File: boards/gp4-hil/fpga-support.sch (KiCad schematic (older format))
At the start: 56 parts, among them J2 XILINX_JTAG, U2 XC7A100T-1FTG256C, U6 W25Q32FW

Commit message: Wired up FPGA config pins, flash, etc
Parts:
- added C143: 4.7 uF, symbol C
- added C144: 0.47 uF, symbol C
- added R119, R120: 1K, symbol R
- added R121, R122, R123, R124, R125, R126, R127, R128, R129, R133, R134: 33, symbol R
- added R130, R131, R132: 4.7K, symbol R
- added R? (x3): 0, symbol R
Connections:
- net 1V0: now also U2.E10 (VCCBRAM), U2.F11 (VCCBRAM), U2.F7 (VCCINT), U2.F9 (VCCINT), U2.G6 (VCCINT), U2.H9 (VCCINT), U2.J6 (VCCINT), U2.K9 (VCCINT), U2.L8 (VCCINT)
- net 1V8: now also C100.1, C104.1, C108.1, C112.1, C87.1, C88.1, C92.1, C96.1, J2.2 (Vccaux), U2.F8 (VCCBATT), U2.G10 (VCCAUX), U2.G8 (VCCADC), U2.J10 (VCCAUX), U2.K11 (VCCAUX), U2.L10 (VCCAUX), U2.L16 (VCCO_14), U2.L6 (VCCO_0), U2.M13 (VCCO_14), U2.N10 (VCCO_14), U2.P7 (VCCO_14), U2.R14 (VCCO_14), U2.T11 (VCCO_14), U6.8 (VCC), C143.2, C144.2, R119.2, R120.2, R130.1, R131.1, R132.1, R?.2
- net 2V5: now also C101.1, C105.1, C109.1, C113.1, C89.1, C93.1, C97.1, U2.A16 (VCCO_15), U2.B13 (VCCO_15), U2.C10 (VCCO_15), U2.E14 (VCCO_15), U2.H15 (VCCO_15), U2.J12 (VCCO_15)
- net DUT_VDD1: now also C103.1, C107.1, C111.1, C115.1, C91.1, C95.1, C99.1, U2.A6 (VCCO_35), U2.B3 (VCCO_35), U2.D7 (VCCO_35), U2.E4 (VCCO_35), U2.F1 (VCCO_35), U2.J2 (VCCO_35)
- net DUT_VDD2: now also C102.1, C106.1, C110.1, C114.1, C90.1, C94.1, C98.1, U2.M3 (VCCO_34), U2.R4 (VCCO_34), U2.T1 (VCCO_34)
- net GND: now also J2.11 (Vss), J2.3 (Vss), J2.5 (Vss), J2.7 (Vss), J2.9 (Vss), U2.E7 (CFGBVS), U2.H7 (XADC_VREF_N), U2.H8 (XADC_VP), U2.J7 (XADC_VN), U2.J8 (XADC_VREF_P), U2.K7 (THERMAL_D_N), U2.K8 (THERMAL_D_P), U6.4 (GND), C143.1, C144.1, R?.2, R?.2
- net FLASH_SCK: now reaches U2.E8 (CCLK)
- net FLASH_SCK: now also R129.2
- net FPGA_DONE: now reaches U2.H10 (DONE)
- net FPGA_DONE: now also R119.1
- net FPGA_INIT_B: now reaches U2.K10 (INIT_B)
- net FPGA_INIT_B: now also R120.1
- net JTAG_TCK: now reaches U2.L7 (TCK)
- net JTAG_TCK: now also J2.6 (TCK)
- net PSU_PGOOD: now reaches U2.L9 (PROG_B)
- net at U2.M10 (M1): now also R?.1
- net at U2.M11 (M2): now also R?.1
- net JTAG_TMS: now reaches U2.M7 (TMS)
- net JTAG_TMS: now also J2.4 (TMS)
- net at U2.M9 (M0): now also R?.1
- net JTAG_TDI: now reaches U2.N7 (TDI)
- net JTAG_TDI: now also J2.10 (TDI_OUT)
- net at U2.N8 (TDO): now also R121.1
- net FLASH_CS_NT: now reaches U6.1 (CS#)
- net FLASH_CS_NT: now also R124.1, R130.2
- net at U6.2 (DO/IO1): now also R122.1
- net at U6.3 (WP#/IO2): now also R123.1
- net at U6.5 (DI/IO0): now also R134.2
- net FLASH_SCKT: now reaches U6.6 (CLK)
- net FLASH_SCKT: now also R129.1
- net at U6.7 (HOLD#/IO3): now also R133.2
- net JTAG_TDO: now reaches J2.8 (TDO_IN)
- net JTAG_TDO: now also R121.2
- new net FLASH_CS_N: R124.2
- new net FLASH_DQ0: R128.2
- new net FLASH_DQ0T: R128.1, R134.1
- new net FLASH_DQ1: R127.2
- new net FLASH_DQ1T: R122.2, R127.1
- new net FLASH_DQ2: R126.2
- new net FLASH_DQ2T: R123.2, R126.1, R132.2
- new net FLASH_DQ3: R125.2
- new net FLASH_DQ3T: R125.1, R131.2, R133.1
- no-connect marks 0 -> 2
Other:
- moved on the sheet: J2

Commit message: Added lots of analog I/O stuff
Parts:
- gave numbers to parts that had none: 3
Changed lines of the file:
@@
 Connection ~ 7750 9250
 $Comp
-L R R?
+L R R135
 U 1 1 57495D86
 P 7200 10750
-F 0 "R?" V 7150 10950 50  0000 C CNN
+F 0 "R135" V 7150 10950 50  0000 C CNN
 F 1 "0" V 7200 10750 50  0000 C CNN
 F 2 "" V 7130 10750 30  0000 C CNN
@@
 	7350 10750 7850 10750
 $Comp
-L R R?
+L R R136
 U 1 1 5749642D
 P 7200 10850
-F 0 "R?" V 7150 11050 50  0000 C CNN
+F 0 "R136" V 7150 11050 50  0000 C CNN
 F 1 "0" V 7200 10850 50  0000 C CNN
 F 2 "" V 7130 10850 30  0000 C CNN
@@
 $EndComp
 $Comp
-L R R?
+L R R137
 U 1 1 57496524
 P 7200 10950
-F 0 "R?" V 7150 11150 50  0000 C CNN
+F 0 "R137" V 7150 11150 50  0000 C CNN
 F 1 "0" V 7200 10950 50  0000 C CNN
 F 2 "" V 7130 10950 30  0000 C CNN

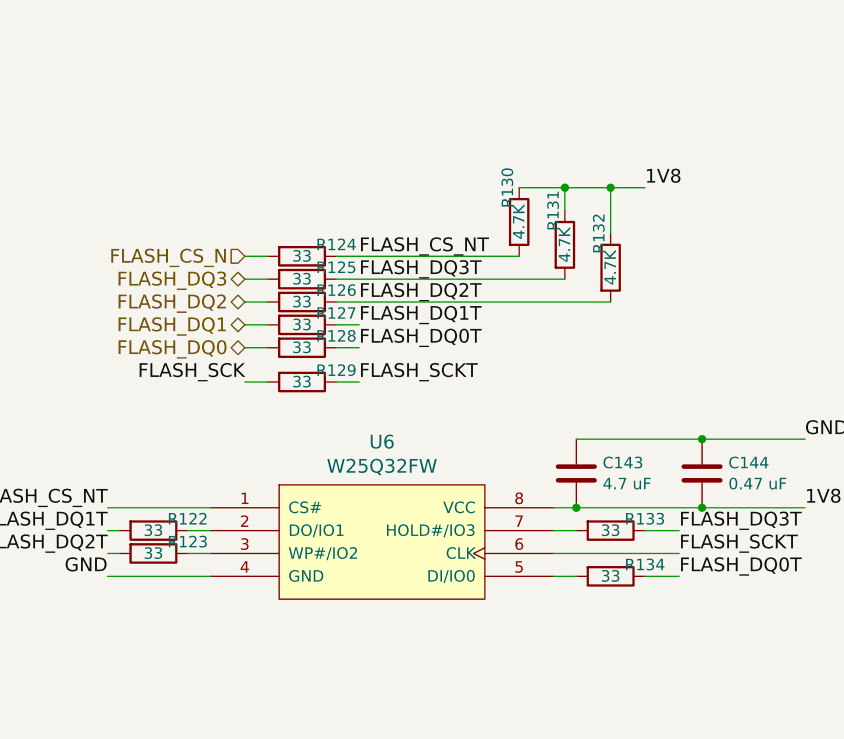
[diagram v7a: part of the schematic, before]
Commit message: Minor refdes placement tweaks
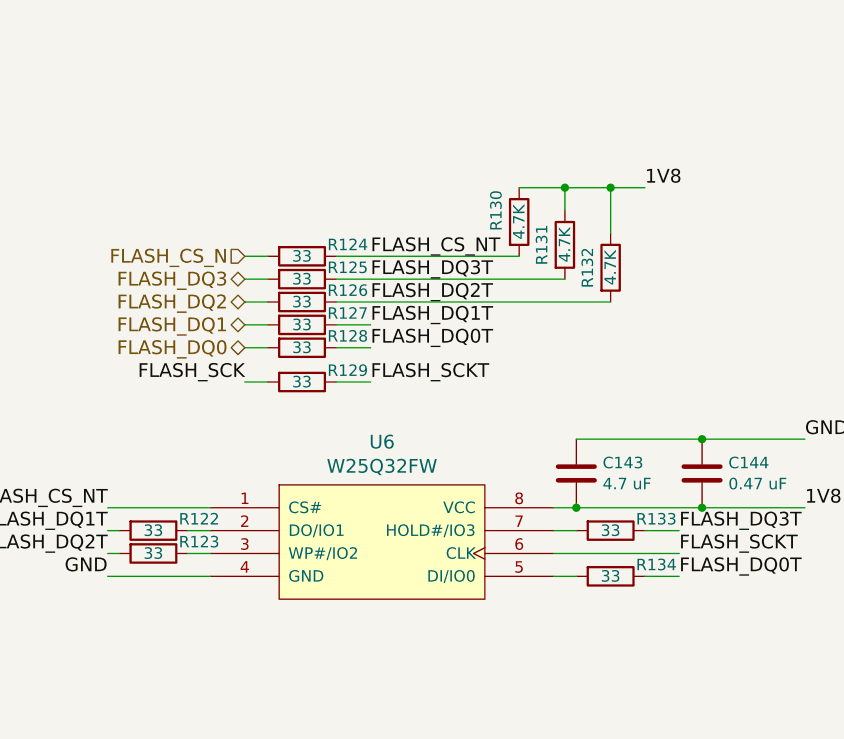
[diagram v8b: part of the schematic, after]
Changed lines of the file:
@@
 U 1 1 5748A020
 P 17550 8600
-F 0 "R122" V 17500 8750 50  0000 C CNN
+F 0 "R122" V 17500 8800 50  0000 C CNN
 F 1 "33" V 17550 8600 50  0000 C CNN
 F 2 "" V 17480 8600 30  0000 C CNN
@@
 U 1 1 5748A79A
 P 17550 8700
-F 0 "R123" V 17500 8850 50  0000 C CNN
+F 0 "R123" V 17500 8900 50  0000 C CNN
 F 1 "33" V 17550 8700 50  0000 C CNN
 F 2 "" V 17480 8700 30  0000 C CNN
@@
 U 1 1 5748A9A0
 P 18200 7400
-F 0 "R124" V 18150 7550 50  0000 C CNN
+F 0 "R124" V 18150 7600 50  0000 C CNN
 F 1 "33" V 18200 7400 50  0000 C CNN
 F 2 "" V 18130 7400 30  0000 C CNN
@@
 U 1 1 5748ACEF
 P 18200 7500
-F 0 "R125" V 18150 7650 50  0000 C CNN
+F 0 "R125" V 18150 7700 50  0000 C CNN
 F 1 "33" V 18200 7500 50  0000 C CNN
 F 2 "" V 18130 7500 30  0000 C CNN
@@
 U 1 1 5748ADFF
 P 18200 7600
-F 0 "R126" V 18150 7750 50  0000 C CNN
+F 0 "R126" V 18150 7800 50  0000 C CNN
 F 1 "33" V 18200 7600 50  0000 C CNN
 F 2 "" V 18130 7600 30  0000 C CNN
@@
 U 1 1 5748AF99
 P 18200 7700
-F 0 "R127" V 18150 7850 50  0000 C CNN
+F 0 "R127" V 18150 7900 50  0000 C CNN
 F 1 "33" V 18200 7700 50  0000 C CNN
 F 2 "" V 18130 7700 30  0000 C CNN
@@
 U 1 1 5748B0B1
 P 18200 7800
-F 0 "R128" V 18150 7950 50  0000 C CNN
+F 0 "R128" V 18150 8000 50  0000 C CNN
 F 1 "33" V 18200 7800 50  0000 C CNN
 F 2 "" V 18130 7800 30  0000 C CNN
@@
 Wire Wire Line
 	17950 7800 18050 7800
-Text Label 18450 7400 0    60   ~ 0
+Text Label 18500 7400 0    60   ~ 0
 FLASH_CS_NT
 Wire Wire Line
 	18350 7400 19150 7400
-Text Label 18450 7500 0    60   ~ 0
+Text Label 18500 7500 0    60   ~ 0
 FLASH_DQ3T
-Text Label 18450 7600 0    60   ~ 0
+Text Label 18500 7600 0    60   ~ 0
 FLASH_DQ2T
-Text Label 18450 7700 0    60   ~ 0
+Text Label 18500 7700 0    60   ~ 0
 FLASH_DQ1T
-Text Label 18450 7800 0    60   ~ 0
+Text Label 18500 7800 0    60   ~ 0
 FLASH_DQ0T
 Wire Wire Line
@@
 	18350 7600 19550 7600
 Wire Wire Line
-	18350 7700 18450 7700
-Wire Wire Line
-	18450 7800 18350 7800
+	18350 7700 18500 7700
+Wire Wire Line
+	18350 7800 18500 7800
 $Comp
 L C C143
@@
 U 1 1 5748DD5A
 P 19550 8600
-F 0 "R133" V 19500 8750 50  0000 C CNN
+F 0 "R133" V 19500 8800 50  0000 C CNN
 F 1 "33" V 19550 8600 50  0000 C CNN
 F 2 "" V 19480 8600 30  0000 C CNN
@@
 U 1 1 5748E267
 P 19550 8800
-F 0 "R134" V 19500 8950 50  0000 C CNN
+F 0 "R134" V 19500 9000 50  0000 C CNN
 F 1 "33" V 19550 8800 50  0000 C CNN
 F 2 "" V 19480 8800 30  0000 C CNN
@@
 U 1 1 5748F616
 P 18200 7950
-F 0 "R129" V 18150 8100 50  0000 C CNN
+F 0 "R129" V 18150 8150 50  0000 C CNN
 F 1 "33" V 18200 7950 50  0000 C CNN
 F 2 "" V 18130 7950 30  0000 C CNN
@@
 Text Label 17950 7950 2    60   ~ 0
 FLASH_SCK
-Text Label 18450 7950 0    60   ~ 0
+Text Label 18500 7950 0    60   ~ 0
 FLASH_SCKT
 Wire Wire Line
-	18450 7950 18350 7950
+	18350 7950 18500 7950
 Text Label 19850 8700 0    60   ~ 0
 FLASH_SCKT
@@
 U 1 1 574915B1
 P 19550 7450
-F 0 "R132" V 19500 7600 50  0000 C CNN
+F 0 "R132" V 19450 7450 50  0000 C CNN
 F 1 "4.7K" V 19550 7450 50  0000 C CNN
 F 2 "" V 19480 7450 30  0000 C CNN
@@
 U 1 1 57491A07
 P 19350 7350
-F 0 "R131" V 19300 7500 50  0000 C CNN
+F 0 "R131" V 19250 7350 50  0000 C CNN
 F 1 "4.7K" V 19350 7350 50  0000 C CNN
 F 2 "" V 19280 7350 30  0000 C CNN
@@
 U 1 1 57492BFD
 P 19150 7250
-F 0 "R130" V 19100 7400 50  0000 C CNN
+F 0 "R130" V 19050 7300 50  0000 C CNN
 F 1 "4.7K" V 19150 7250 50  0000 C CNN
 F 2 "" V 19080 7250 30  0000 C CNN
